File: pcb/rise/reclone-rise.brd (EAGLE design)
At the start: 85 x 56 mm, 130 parts, among them Y1 12MHz

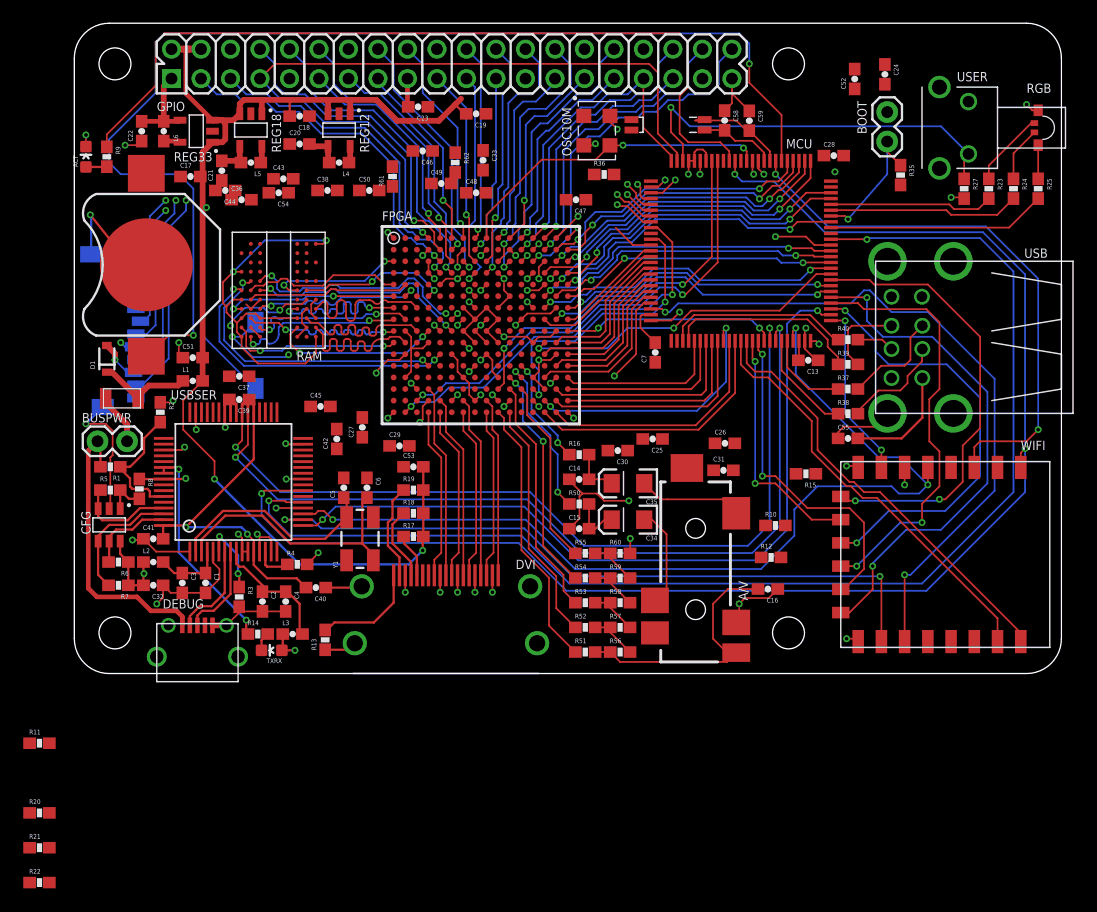
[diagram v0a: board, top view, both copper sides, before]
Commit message: Cleaned up a few things: TCK, resistor placement, and a couple vias
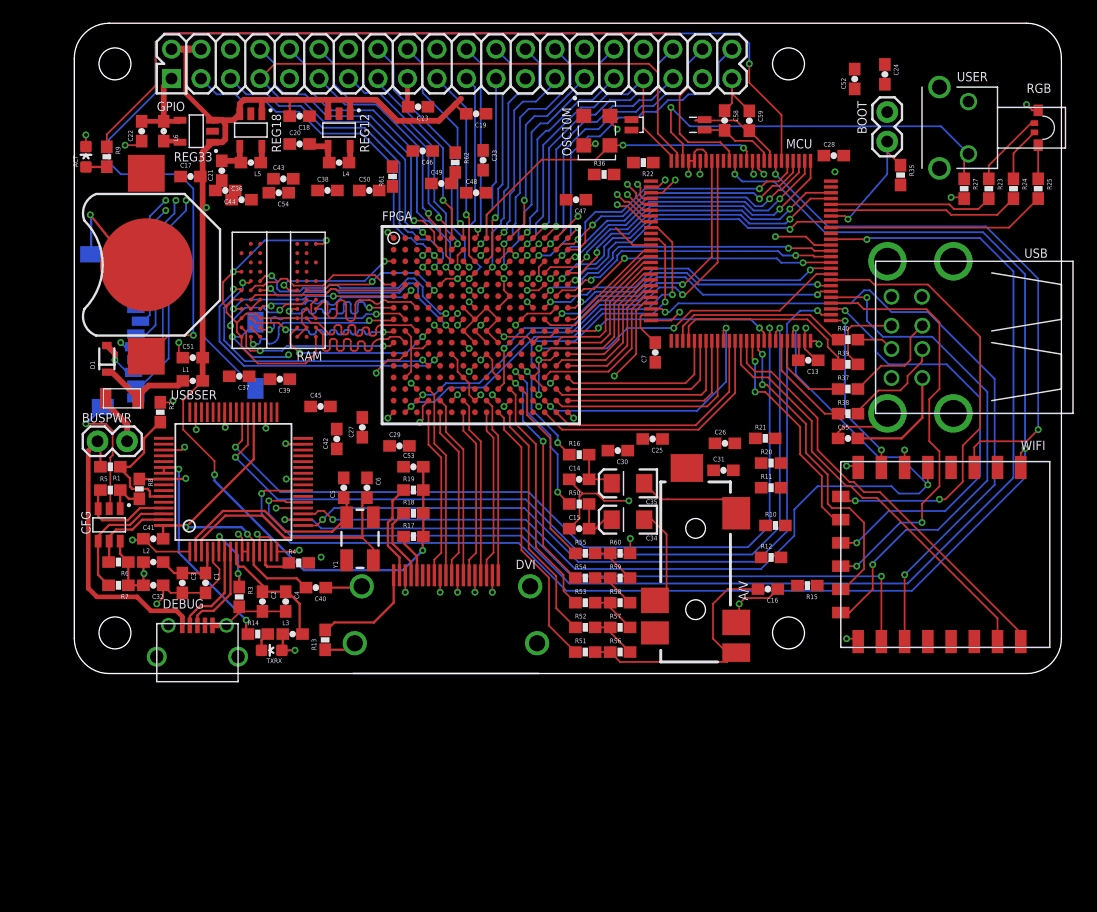
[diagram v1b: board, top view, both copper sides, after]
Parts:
- moved R22 80.9 mm to (49.0, 44.0), turned to 180 degrees
- moved R21 71.8 mm to (59.5, 20.2)
- moved R20 69.8 mm to (60.0, 18.1)
- moved R11 66.7 mm to (60.0, 16.0)
- moved R15 9.63 mm to (63.1, 7.58)
- moved C39 3.91 mm to (17.7, 25.4)
- moved R4 0.18 mm to (19.3, 9.53)
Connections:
- removed net N$118: FPGA.M14
- removed net N$38: FPGA.N8
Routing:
- net JTAG_TCK: track 46.2 -> 106.5 mm, vias 3 -> 4
- net SDIO_D1: track 28.9 -> 27.2 mm
- net SDIO_D0: track 21.0 -> 19.4 mm
- net +3V3: track 76.4 -> 75.0 mm
- net JTAG_FPGA_TDO: track 44.8 -> 43.6 mm
- net GND: track 161.3 -> 162.4 mm, vias 52 -> 53
- net /RESET: track 127.8 -> 127.0 mm
- net JTAG_TRST: track 110.0 -> 109.2 mm
- net M3CASN: track 19.5 -> 20.2 mm
- net N$20: track 18.7 -> 18.2 mm

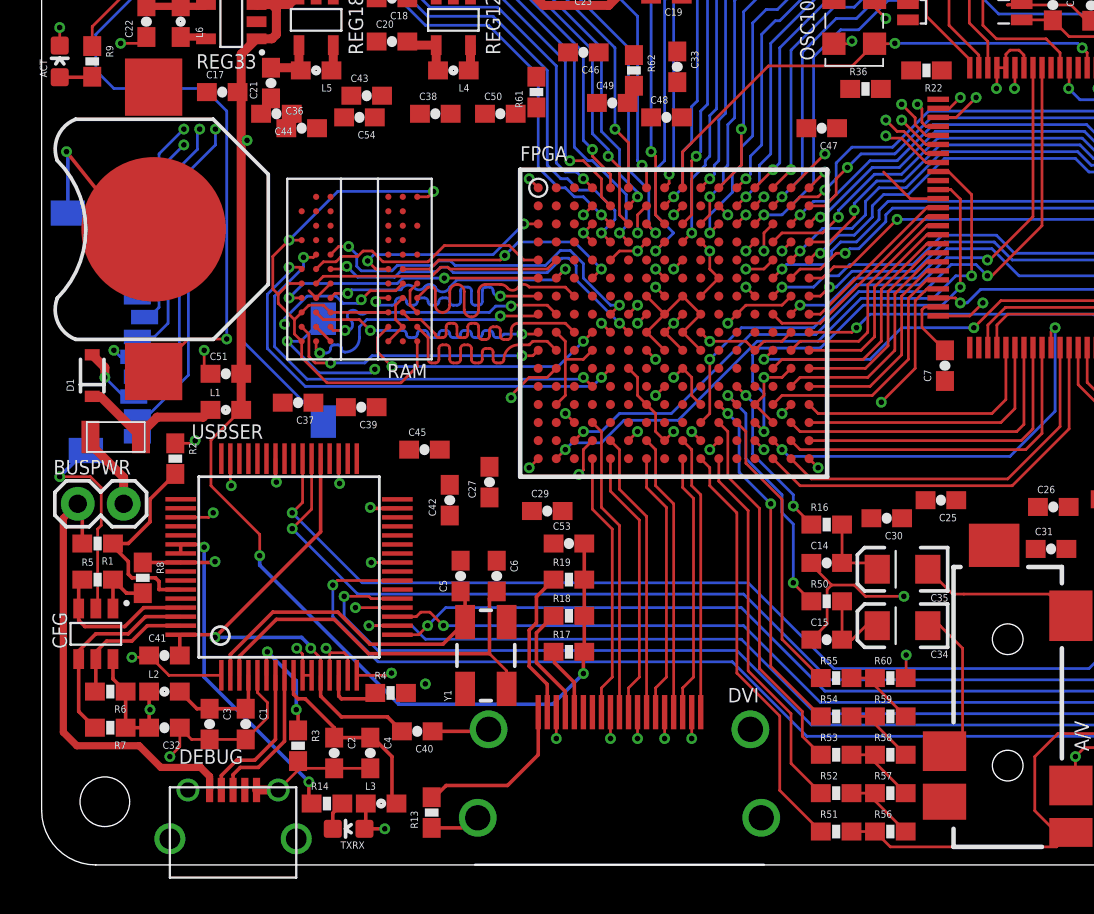
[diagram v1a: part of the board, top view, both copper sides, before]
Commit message: Finished FPGA escape routing for remaining DDR2 lines
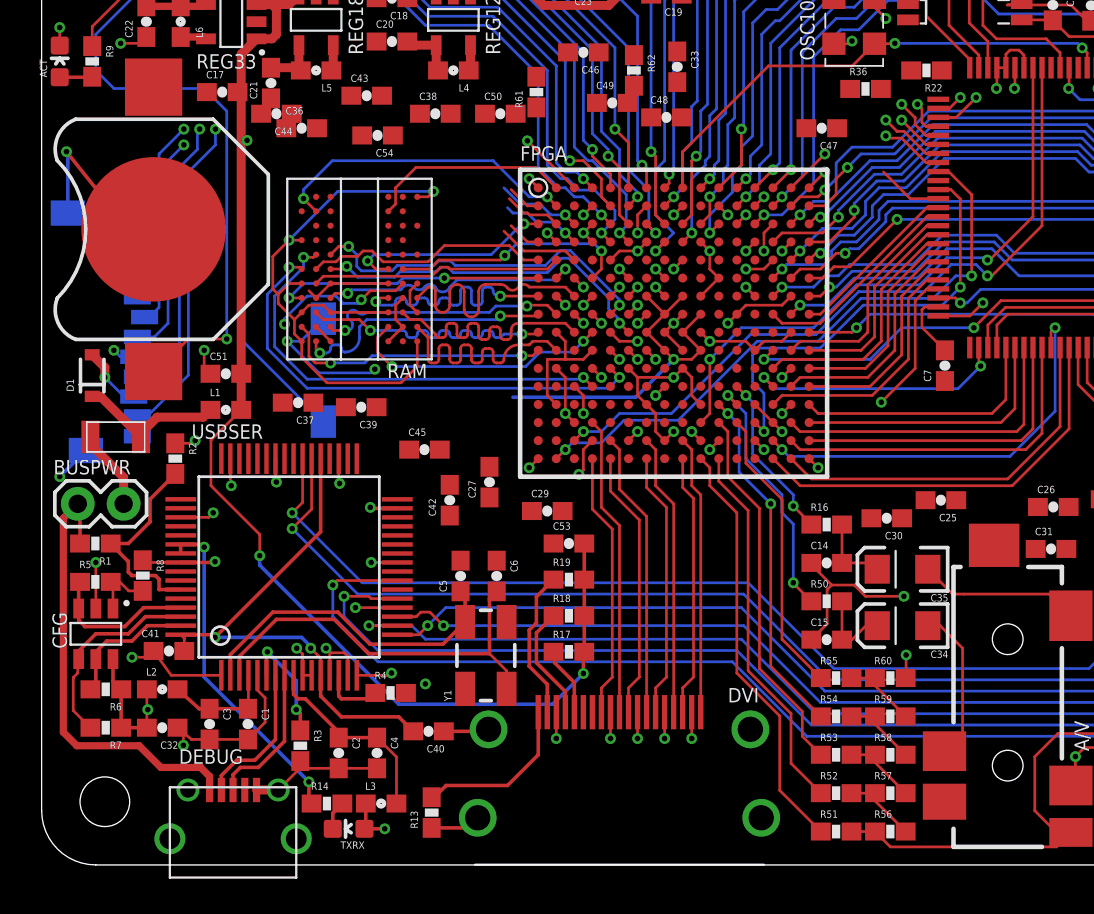
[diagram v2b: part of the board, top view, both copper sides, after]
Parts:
- moved C54 1.41 mm to (18.6, 40.4)
- moved C40 0.62 mm to (21.4, 7.40)
- moved C4 0.38 mm to (18.6, 6.20)
- moved C41 0.35 mm to (7.05, 11.8)
- moved R6 0.28 mm to (3.55, 9.72)
- moved C2 0.25 mm to (16.4, 6.20)
- moved R7 0.25 mm to (3.55, 7.60)
- moved L2 0.18 mm to (6.67, 9.72)
- moved R5 0.18 mm to (2.98, 15.7)
- moved C1 0.12 mm to (11.4, 7.80)
- moved C32 0.12 mm to (6.67, 7.60)
- moved R1 0.12 mm to (2.98, 17.8)
- moved R3 0.12 mm to (14.3, 6.60)
- moved R8 0.12 mm to (5.60, 16.0)
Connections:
- net FPGA_INT: now also FPGA.M14, MCU.52; no longer MCU.35
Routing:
- net DDR2_VREF: track 7.99 -> 57.7 mm, vias 2 -> 4
- net M3A8: track 0.00 -> 17.2 mm, vias 0 -> 2
- net +1V8: track 38.7 -> 53.7 mm, vias 2 -> 4
- net FPGA_INT: track 0.00 -> 14.6 mm, vias 0 -> 2
- net M3A0: track 0.00 -> 14.3 mm, vias 0 -> 1
- net M3A1: track 0.00 -> 13.1 mm, vias 0 -> 1
- net M3A9: track 0.00 -> 11.3 mm
- net M3A5: track 0.00 -> 11.0 mm, vias 0 -> 1
- net M3A3: track 0.00 -> 11.0 mm, vias 0 -> 1
- net +5V/4: track 13.0 -> 23.8 mm, vias 0 -> 1
- net M3A10: track 0.00 -> 10.0 mm, vias 0 -> 1
- net M3A4: track 0.00 -> 9.37 mm, vias 0 -> 1
- net M3A13: track 0.00 -> 7.91 mm, vias 0 -> 1
- net M3A6: track 0.00 -> 7.85 mm, vias 0 -> 1
- net M3A12: track 0.00 -> 7.54 mm, vias 0 -> 1
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
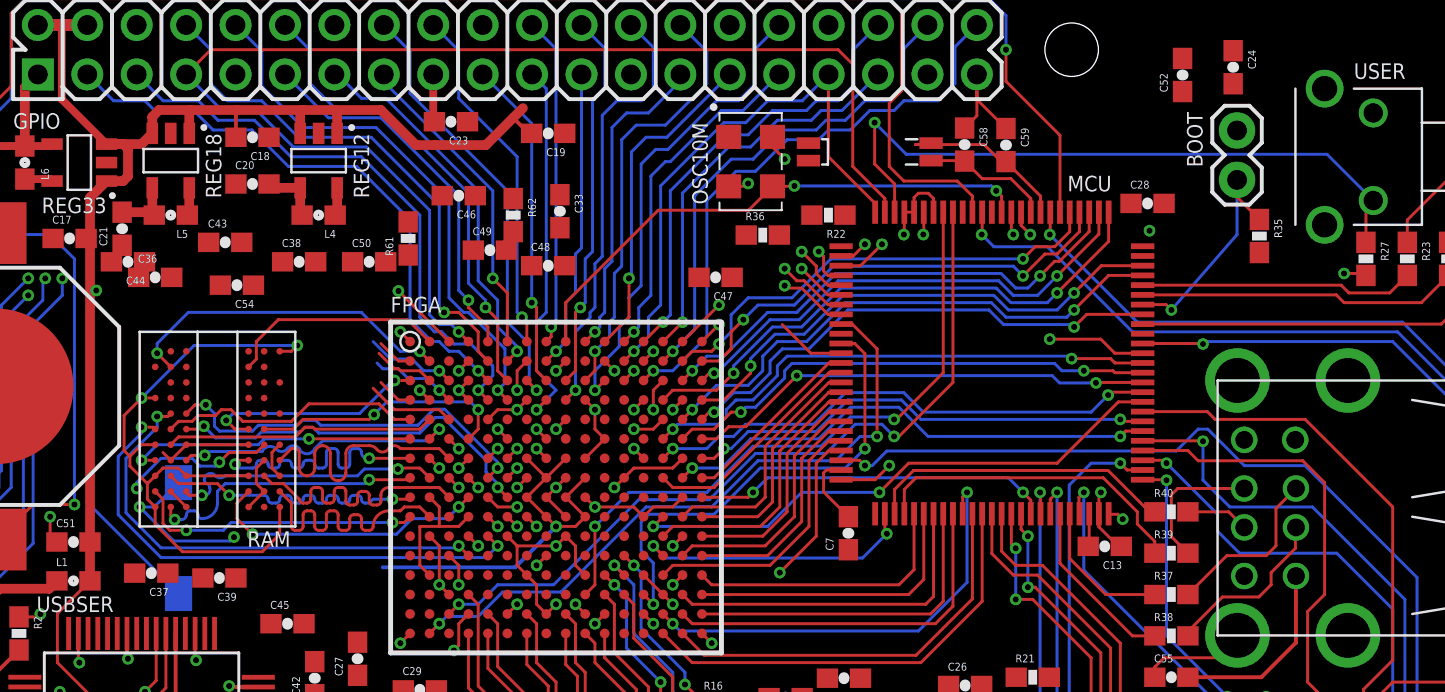
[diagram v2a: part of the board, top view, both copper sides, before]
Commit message: Routed some DDR2 power and address lines
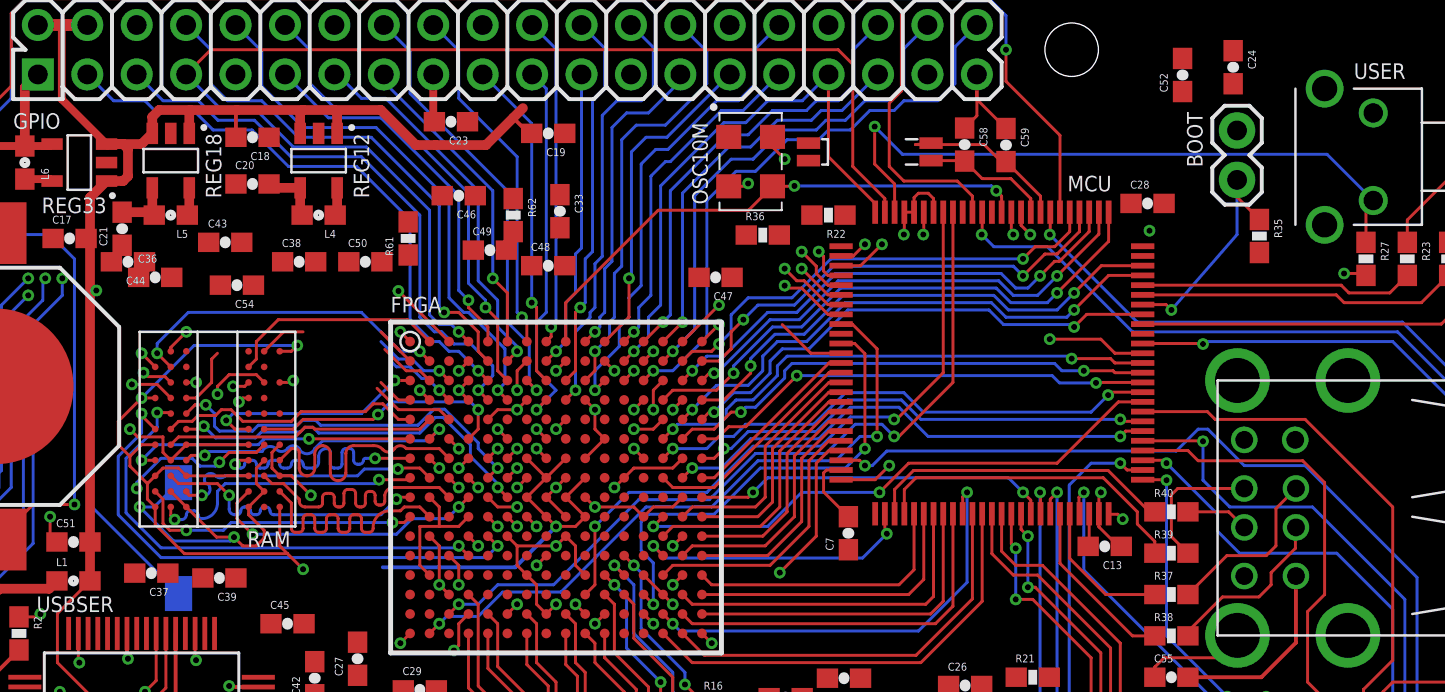
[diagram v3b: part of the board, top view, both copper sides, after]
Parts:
- moved C50 0.20 mm to (25.2, 41.6)
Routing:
- net M3A0: track 14.3 -> 27.8 mm, vias 1 -> 2
- net GND: track 157.3 -> 168.6 mm, vias 55 -> 58
- net M3A3: track 11.0 -> 22.0 mm, vias 1 -> 2
- net M3A6: track 7.85 -> 18.6 mm, vias 1 -> 2
- net +5V/3: track 36.3 -> 44.9 mm, vias 2 -> 4
- net M3A5: track 11.0 -> 19.3 mm, vias 1 -> 2
- net M3A13: track 7.91 -> 16.0 mm, vias 1 -> 2
- net M3A1: track 13.1 -> 20.3 mm, vias 1 -> 2
- net M3A2: track 1.87 -> 5.13 mm
- net M3A12: track 7.54 -> 9.65 mm
- net M3ODT: track 27.1 -> 28.2 mm
- net M3A4: track 9.37 -> 10.4 mm, vias 1 -> 2
- net M3A10: track 10.0 -> 11.0 mm
- net +1V8: track 53.7 -> 52.8 mm
- net M3A7: track 4.49 -> 3.83 mm

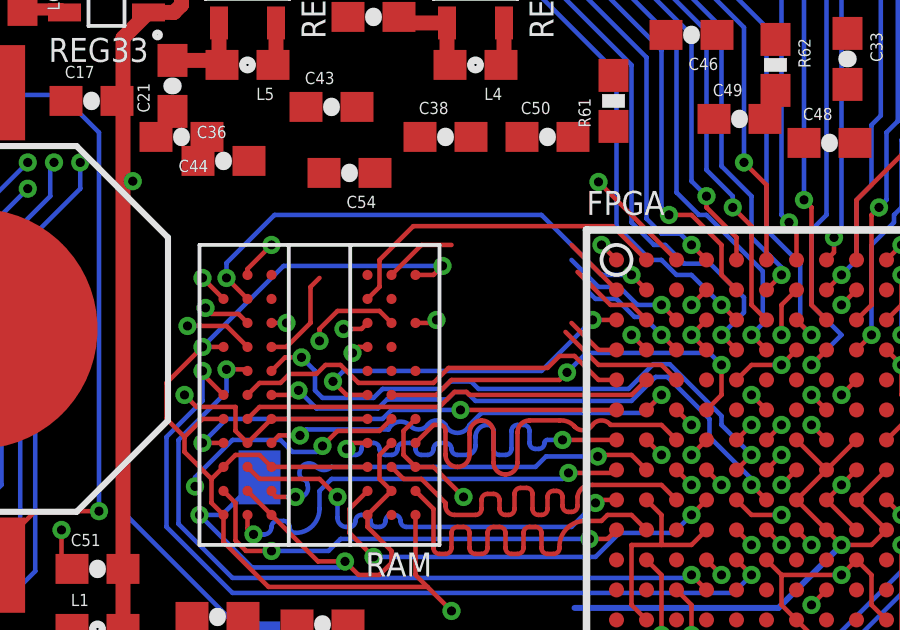
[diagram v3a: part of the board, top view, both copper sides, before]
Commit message: Fixed +1V8 and +1V2 power supply symbols
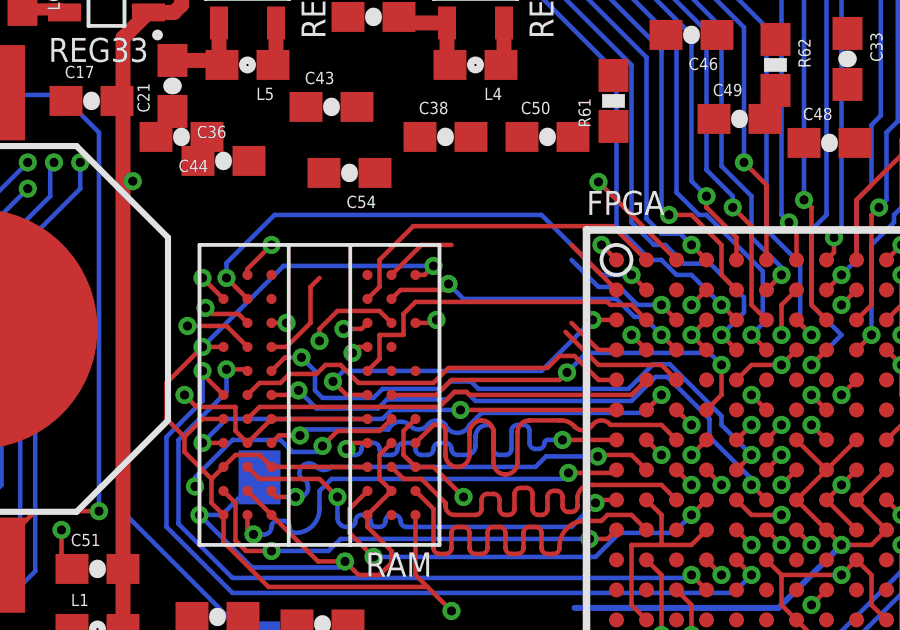
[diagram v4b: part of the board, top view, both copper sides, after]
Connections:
- net +5V/4 renamed +1V2
- removed net +5V/3: RAM.A1, RAM.A9, RAM.C1, RAM.C3, RAM.C7, RAM.C9, RAM.E1, RAM.E9, RAM.H9, RAM.L1
- net +1V8: now also RAM.A1, RAM.A9, RAM.C1, RAM.C3, RAM.C7, RAM.C9, RAM.E1, RAM.E9, RAM.H9, RAM.L1
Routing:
- net +5V/3: track 44.9 -> 0.00 mm, vias 4 -> 0
- net +1V8: track 52.8 -> 97.1 mm, vias 4 -> 8
- net M3BA1: track 2.96 -> 11.4 mm
- net M3A7: track 3.83 -> 10.6 mm, vias 1 -> 2
